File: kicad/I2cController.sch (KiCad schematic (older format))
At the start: 39 parts, among them J1 CONN_02X01, J2 CONN_02X01, J3 CONN_02X01, J4 CONN_01X06, J5 CONN_02X01, J6 CONN_02X01, Q1 Q_NPN_BCE, SW1 Rotary_Encoder_Switch, SW2 SW_Push, SW3 SW_Push, SW4 SW_Push, SW5 SW_Push, SW6 SW_Push, U1 MCP23017

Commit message: Schematic update
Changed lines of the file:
@@
 LIBS:power
 LIBS:device
-LIBS:transistors
-LIBS:conn
 LIBS:linear
 LIBS:regul
-LIBS:74xx
-LIBS:cmos4000
 LIBS:adc-dac
 LIBS:memory
@@
 LIBS:digital-audio
 LIBS:philips
-LIBS:display
 LIBS:cypress
 LIBS:siliconi
@@
 LIBS:atmel
 LIBS:contrib
-LIBS:valves
 LIBS:w_connectors
 LIBS:max6675
 LIBS:lcd16x2
-LIBS:switches
 LIBS:HotAirGun-cache
 EELAYER 26 0
@@
 	2850 6590 2850 6640
 Wire Wire Line
-	3950 5790 3950 5840
-Wire Wire Line
-	3450 5790 3450 5840
-Wire Wire Line
 	3450 6140 3450 6190
 Wire Wire Line
@@
 MCP_INT
 Connection ~ 8050 3075
+Wire Wire Line
+	3450 5840 3450 5790
+Wire Wire Line
+	3950 5840 3950 5790
 $EndSCHEMATC

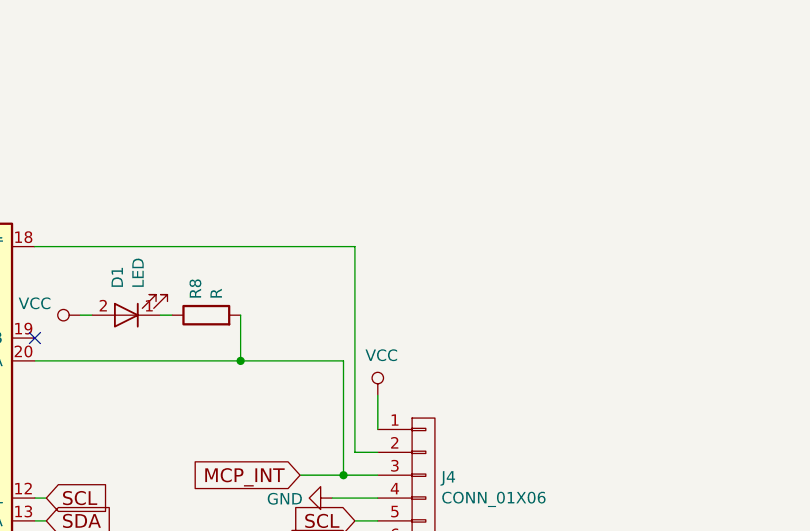
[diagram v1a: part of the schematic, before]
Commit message: Modified the Kicad schematic adding the reset to I2c controller
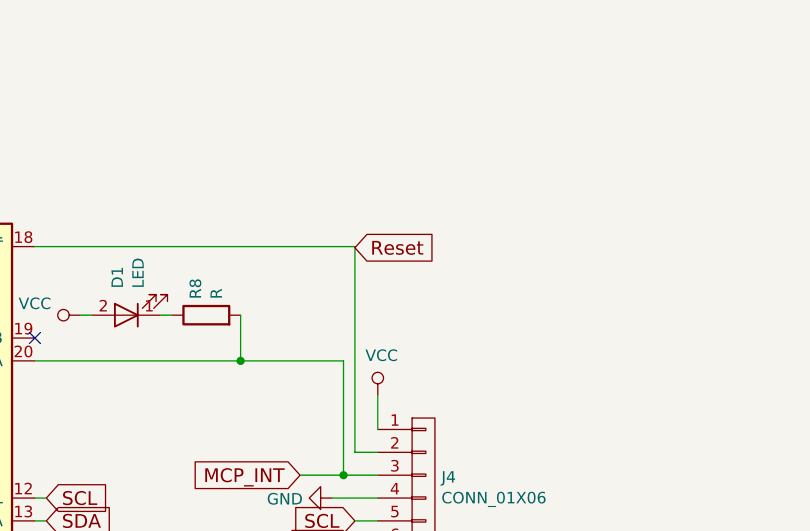
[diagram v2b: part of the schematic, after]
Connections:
- net labels added: Reset
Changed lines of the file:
@@
-EESchema Schematic File Version 3
+EESchema Schematic File Version 2
 LIBS:HotAirGun-rescue
 LIBS:power
 LIBS:device
+LIBS:transistors
+LIBS:conn
 LIBS:linear
 LIBS:regul
+LIBS:74xx
+LIBS:cmos4000
 LIBS:adc-dac
 LIBS:memory
@@
 LIBS:digital-audio
 LIBS:philips
+LIBS:display
 LIBS:cypress
 LIBS:siliconi
@@
 LIBS:atmel
 LIBS:contrib
-LIBS:w_connectors
+LIBS:valves
 LIBS:max6675
 LIBS:lcd16x2
+LIBS:switches
 LIBS:HotAirGun-cache
-EELAYER 26 0
+EELAYER 25 0
 EELAYER END
 $Descr A4 11693 8268
@@
 Wire Wire Line
 	3950 5840 3950 5790
+Text GLabel 8100 2080 2    60   Input ~ 0
+Reset
 $EndSCHEMATC

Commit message: v2
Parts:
- removed J1, J2, J3, J5, J6: CONN_02X01, Pin_Headers:Pin_Header_Straight_1x02_Pitch2.54mm, symbol Conn_02x01
- removed J4: CONN_01X06, Pin_Headers:Pin_Header_Straight_1x06_Pitch2.54mm, symbol CONN_01X06
- removed LD1: 5V Rd, symbol LED-RESCUE-HotAirGun
- removed LD2: 12V Gr, symbol LED-RESCUE-HotAirGun
- removed LD3: Rd, symbol LED-RESCUE-HotAirGun
- removed LD4: Gr, symbol LED-RESCUE-HotAirGun
- removed Q1: Q_NPN_BCE, TO_SOT_Packages_THT:TO-92_Rugged_Reverse, symbol Q_NPN_BCE
- removed R10: R, Resistors_SMD:R_0805_HandSoldering, symbol R
- removed R11, R13, R14: 470R, symbol R
- removed R12: 1K, symbol R
- removed R15, R16: 6K8, symbol R
- removed SW1: Rotary_Encoder_Switch, rotary_encoder:SF-ROTARY-ENCODER, symbol Rotary_Encoder_Switch
- removed SW4, SW5, SW6: SW_Push, Buttons_Switches_THT:SW_PUSH_6mm_h7.3mm, symbol SW_Push
- removed Start1: ~, symbol CONN_01X01
- removed Stop1: ~, symbol CONN_01X02
- added BZ1: Buzzer, Buzzers_Beepers:Buzzer_12x9.5RM7.6, symbol Buzzer
- added D2: LED, LEDs:LED-3MM, symbol LED
- added J1: CONN_02X03, Pin_Headers:Pin_Header_Straight_2x03, symbol CONN_02X03
- added J2: CONN_01X06, Pin_Headers:Pin_Header_Straight_1x06, symbol CONN_01X06
- added J3: CONN_02X02, Pin_Headers:Pin_Header_Straight_2x02, symbol CONN_02X02
- added Q1: Q_NPN_CBE, TO_SOT_Packages_THT:TO-92_Rugged, symbol Q_NPN_CBE
- added SW1: Start, Buttons_Switches_THT:SW_PUSH_SMALL, symbol SW_Push
- added SW4: Rotary_Encoder_Switch_V2, Rotary_Encoder_Switch_V2, symbol Rotary_Encoder_Switch_V2
- D1: footprint LEDs:LED_D5.0mm -> LEDs:LED-3MM
- DS1: footprint Displays:WC1602A -> Display:WC1602A
- R1: value R -> 470R; footprint Resistors_SMD:R_0805_HandSoldering -> Discret:R3
- R2, R3: value R -> 470R; footprint Resistors_SMD:R_0805_HandSoldering -> Resistors_SMD:R_0603_HandSoldering
- R4, R5: value R -> 10K; footprint Resistors_SMD:R_0805_HandSoldering -> Resistors_SMD:R_0603_HandSoldering
- R6: value R -> 10K; footprint Resistors_THT:R_Axial_DIN0204_L3.6mm_D1.6mm_P7.62mm_Horizontal -> Resistors_SMD:R_0603_HandSoldering
- R7: value R -> 360R; footprint Resistors_SMD:R_0805_HandSoldering -> Resistors_SMD:R_0603_HandSoldering
- R8, R9: value R -> 8K2; footprint Resistors_SMD:R_0805_HandSoldering -> Resistors_SMD:R_0603_HandSoldering
- RV1: footprint Potentiometers:Potentiometer_Trimmer_ACP_CA6h_Vertical -> Potentiometers:Potentiometer_VishaySpectrol-Econtrim-Type36M
- SW2: value SW_Push -> Stop; footprint Buttons_Switches_THT:SW_PUSH_6mm_h7.3mm -> Buttons_Switches_THT:SW_PUSH_SMALL
- SW3: value SW_Push -> WeldCurv; footprint Buttons_Switches_THT:SW_PUSH_6mm_h7.3mm -> Buttons_Switches_THT:SW_PUSH_SMALL
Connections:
- net labels added: Buz, Gnd_P, Led, Start, Stop, Vcc_P, WeldCurv
- net labels removed: +12V, A6, A7, GND, MCP_INT, RB2, RB6, Reset, SCL, SDA, VCC
- wire segments 119 -> 62
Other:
- moved on the sheet: DS1, R1, U1

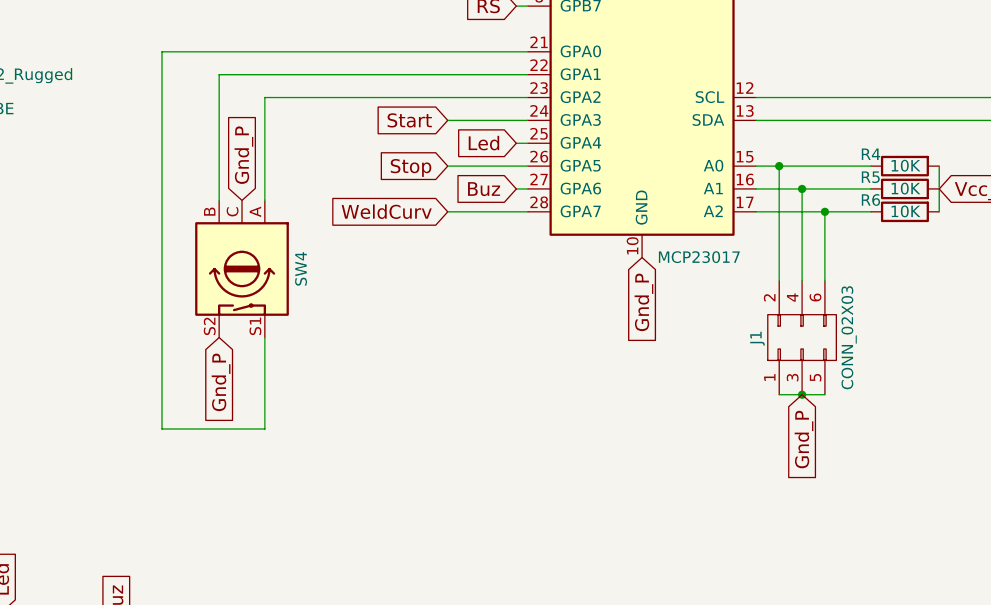
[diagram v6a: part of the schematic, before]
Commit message: New PCB version with smd component Added plot folder with gerber file
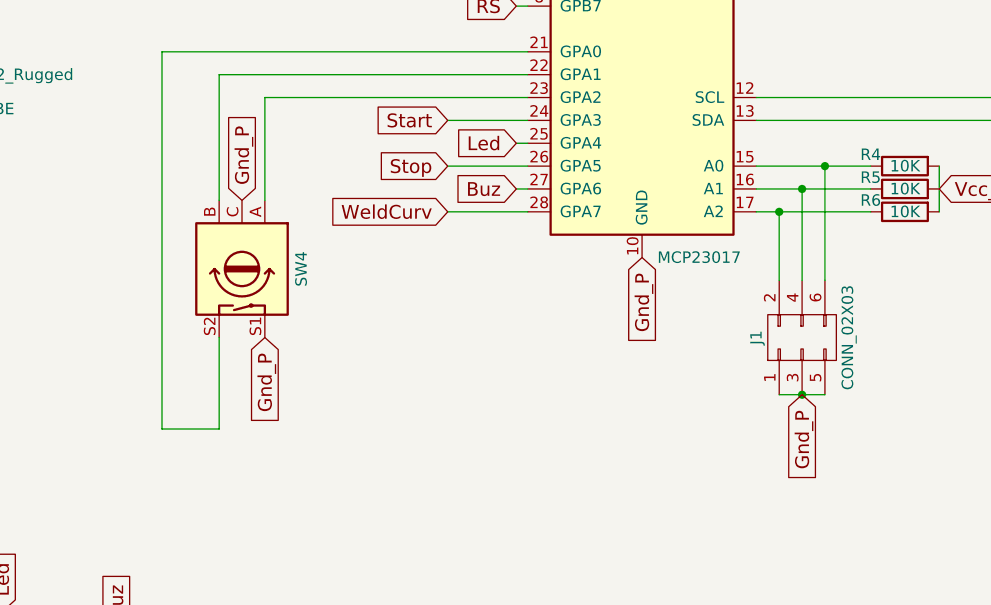
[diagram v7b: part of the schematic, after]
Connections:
- net Gnd_P: now also SW4.S1; no longer SW4.S2
- net at R4.1, U1.15 (A0): now also J1.6 (P6); no longer J1.2 (P2)
- net at R6.1, U1.17 (A2): now also J1.2 (P2); no longer J1.6 (P6)
- net at U1.21 (GPA0): now also SW4.S2; no longer SW4.S1
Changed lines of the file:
@@
 Text GLabel 2800 5800 3    60   Input ~ 0
 Gnd_P
-Text GLabel 4450 4000 3    60   Input ~ 0
+Text GLabel 4650 4000 3    60   Input ~ 0
 Gnd_P
 Text GLabel 4550 3400 1    60   Input ~ 0
@@
 Text GLabel 3500 5200 1    60   Input ~ 0
 Led
-Wire Wire Line
-	6900 3750 6900 3250
-Connection ~ 6900 3250
-Wire Wire Line
-	7100 3750 7100 3450
-Connection ~ 7100 3450
 Connection ~ 7950 2950
 Connection ~ 8100 3050
@@
 Connection ~ 3500 5800
 Wire Wire Line
-	4200 4400 4650 4400
+	4450 4400 4450 4000
 Wire Wire Line
-	4650 4400 4650 4000
+	4200 4400 4450 4400
+Wire Wire Line
+	6900 3450 6900 3750
+Connection ~ 6900 3450
+Wire Wire Line
+	7100 3750 7100 3250
+Connection ~ 7100 3250
 $EndSCHEMATC

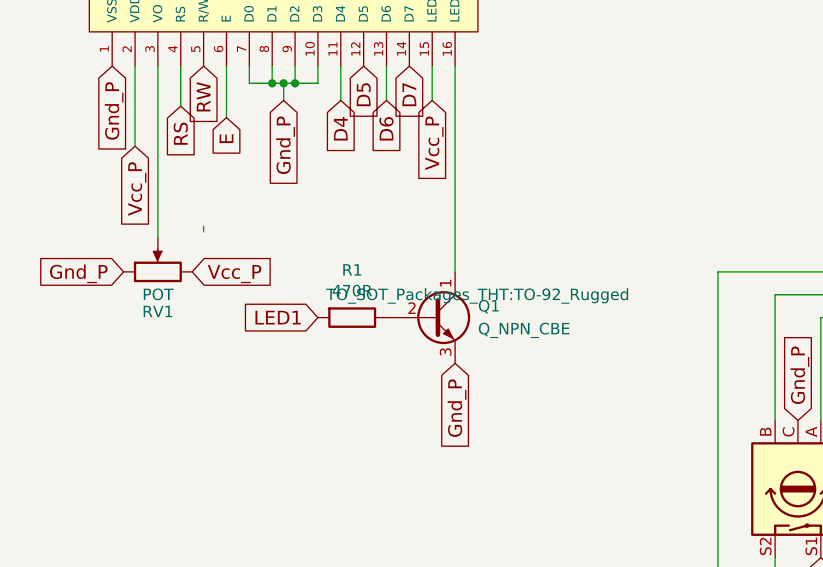
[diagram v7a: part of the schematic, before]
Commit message: Update with new PCB version
Kicad schematic and pcb layout correction on Mosfet and Triac footprint.
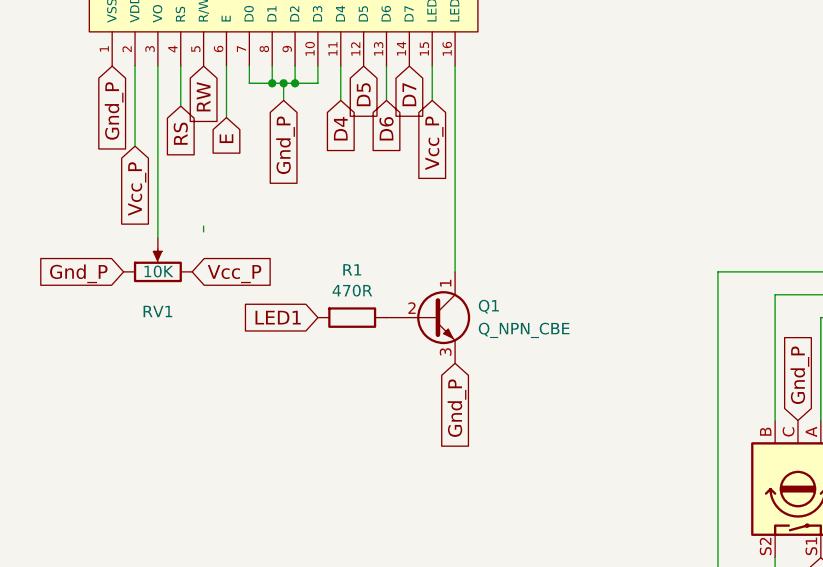
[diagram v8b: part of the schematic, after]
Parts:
- D1, D2: footprint LEDs:LED-3MM -> LEDs:LED-5MM
- Q1: footprint TO_SOT_Packages_THT:TO-92_Rugged -> TO_SOT_Packages_THT:TO-92_Rugged_Reverse
- RV1: value POT -> 10K
- SW4: footprint Rotary_Encoder_Switch_V2 -> Rotary_Encoder:RotaryEncoder_Alps_EC11E-Switch_Vertical_H20mm
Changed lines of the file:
@@
 F 0 "D2" H 7350 2200 50  0000 C CNN
 F 1 "LED" H 7350 2000 50  0000 C CNN
-F 2 "LEDs:LED-3MM" H 7350 2100 50  0001 C CNN
+F 2 "LEDs:LED-5MM" H 7350 2100 50  0001 C CNN
 F 3 "" H 7350 2100 50  0001 C CNN
 	1    7350 2100
@@
 P 1750 2750
 F 0 "RV1" V 1575 2750 50  0000 C CNN
-F 1 "POT" V 1650 2750 50  0000 C CNN
+F 1 "10K" V 1750 2750 50  0000 C CNN
 F 2 "Potentiometers:Potentiometer_VishaySpectrol-Econtrim-Type36M" H 1750 2750 50  0001 C CNN
 F 3 "" H 1750 2750 50  0001 C CNN
@@
 F 0 "D1" H 3500 5750 50  0000 C CNN
 F 1 "LED" H 3500 5550 50  0000 C CNN
-F 2 "LEDs:LED-3MM" H 3500 5650 50  0001 C CNN
+F 2 "LEDs:LED-5MM" H 3500 5650 50  0001 C CNN
 F 3 "" H 3500 5650 50  0000 C CNN
 	1    3500 5650
@@
 F 0 "SW4" H 4550 3960 50  0000 C CNN
 F 1 "Rotary_Encoder_Switch_V2" H 4550 3440 50  0001 C CNN
-F 2 "Rotary_Encoder_Switch_V2" H 4450 3860 50  0001 C CNN
+F 2 "Rotary_Encoder:RotaryEncoder_Alps_EC11E-Switch_Vertical_H20mm" H 4450 3860 50  0001 C CNN
 F 3 "" H 4550 3960 50  0001 C CNN
 	1    4550 3700
@@
 F 0 "Q1" H 3150 3000 50  0000 L CNN
 F 1 "Q_NPN_CBE" H 3150 2900 50  0000 L CNN
-F 2 "TO_SOT_Packages_THT:TO-92_Rugged" H 3150 3050 50  0000 C CNN
+F 2 "TO_SOT_Packages_THT:TO-92_Rugged_Reverse" H 3150 3050 50  0001 C CNN
 F 3 "" H 2950 2950 50  0000 C CNN
 	1    2950 2950
